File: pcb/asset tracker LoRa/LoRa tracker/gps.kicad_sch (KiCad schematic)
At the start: 7 parts

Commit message: pcb kastje
pcb in kastje getekend
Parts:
- AE1: footprint connectors_user:sma_right angeld -> connectors_user:sma juist
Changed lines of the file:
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@@
       (effects (font (size 1.27 1.27)) (justify left))
     )
-    (property "Footprint" "connectors_user:sma_right angeld" (id 2) (at 184.15 55.88 0)
+    (property "Footprint" "connectors_user:sma juist" (id 2) (at 184.15 55.88 0)
       (effects (font (size 1.27 1.27)) hide)
     )

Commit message: lora tracker
lora tracker afgemaakt
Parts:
- AE1: footprint connectors_user:sma juist -> connectors_user:ufl connector
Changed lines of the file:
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@@
   (no_connect (at 111.76 66.04))
   (no_connect (at 143.51 81.28))
+  (bus_entry (at 234.95 41.91) (size 2.54 2.54)
+    (stroke (width 0.1524) (type solid) (color 0 0 0 0))
+  )
   (wire (pts (xy 72.39 58.42) (xy 77.47 58.42))
     (stroke (width 0) (type solid) (color 0 0 0 0))
@@
       (effects (font (size 1.27 1.27)) (justify left))
     )
-    (property "Footprint" "connectors_user:sma juist" (id 2) (at 184.15 55.88 0)
-      (effects (font (size 1.27 1.27)) hide)
-    )
+    (property "Footprint" "connectors_user:ufl connector" (id 2) (at 184.15 55.88 0)
+      (effects (font (size 1.27 1.27)) hide)
+    )

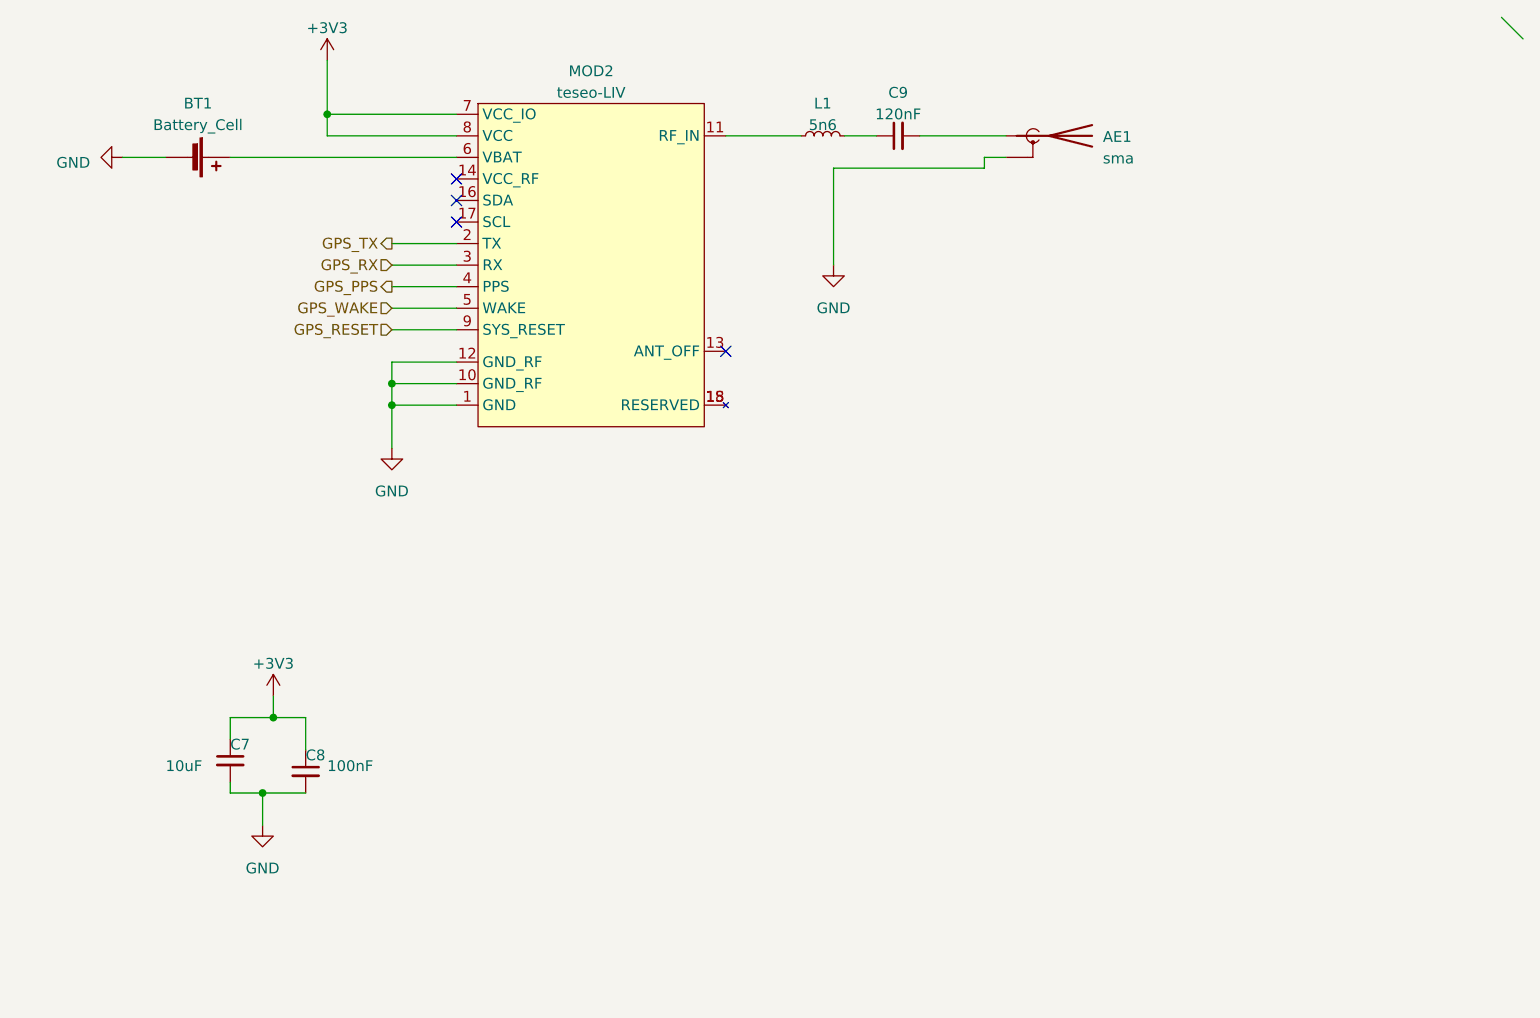
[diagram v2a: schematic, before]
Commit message: versie2
aan versie 2 begonnen met tekenen en code beginnen schrijven voor quadkey
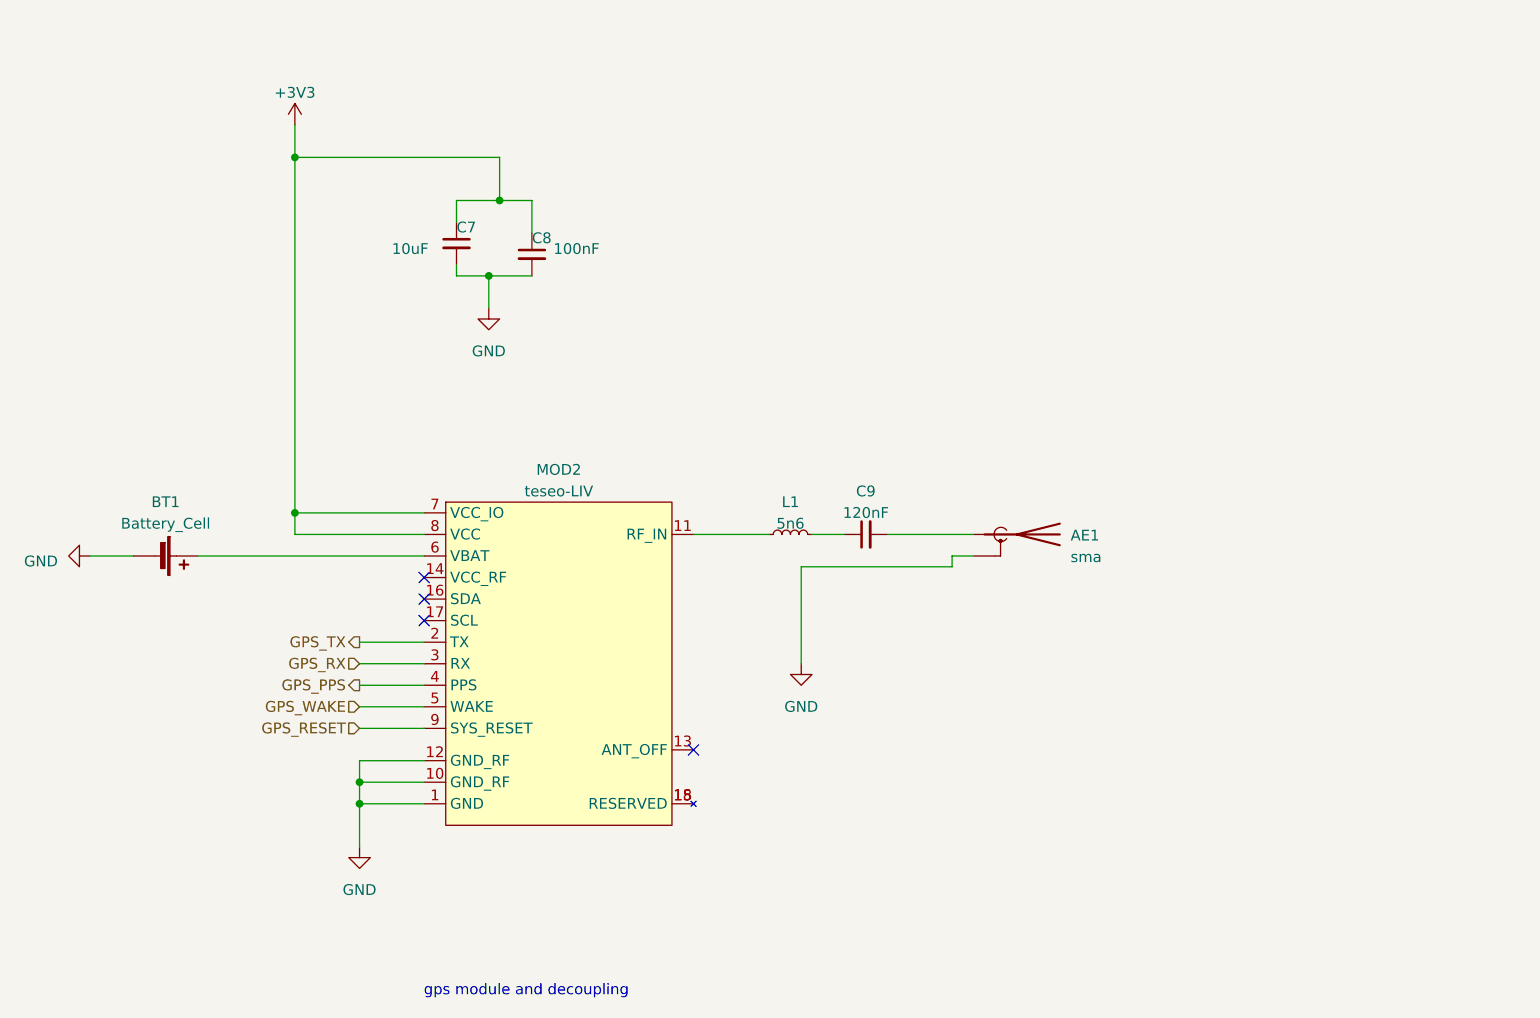
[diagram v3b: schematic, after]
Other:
- note added: "gps module and decoupling"
- moved on the sheet: AE1, BT1, C7, C8, C9, L1, MOD2
